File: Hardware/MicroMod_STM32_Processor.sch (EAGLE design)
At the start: 40 parts, among them J1 MICROMOD-2222, Q1 MOSFET_PCH-DMG2305UX-7, U1 STM32F405RGT6, U3 W25QXX128MBIT-6X5, Y1 12MHz, Y2 32.768kHz

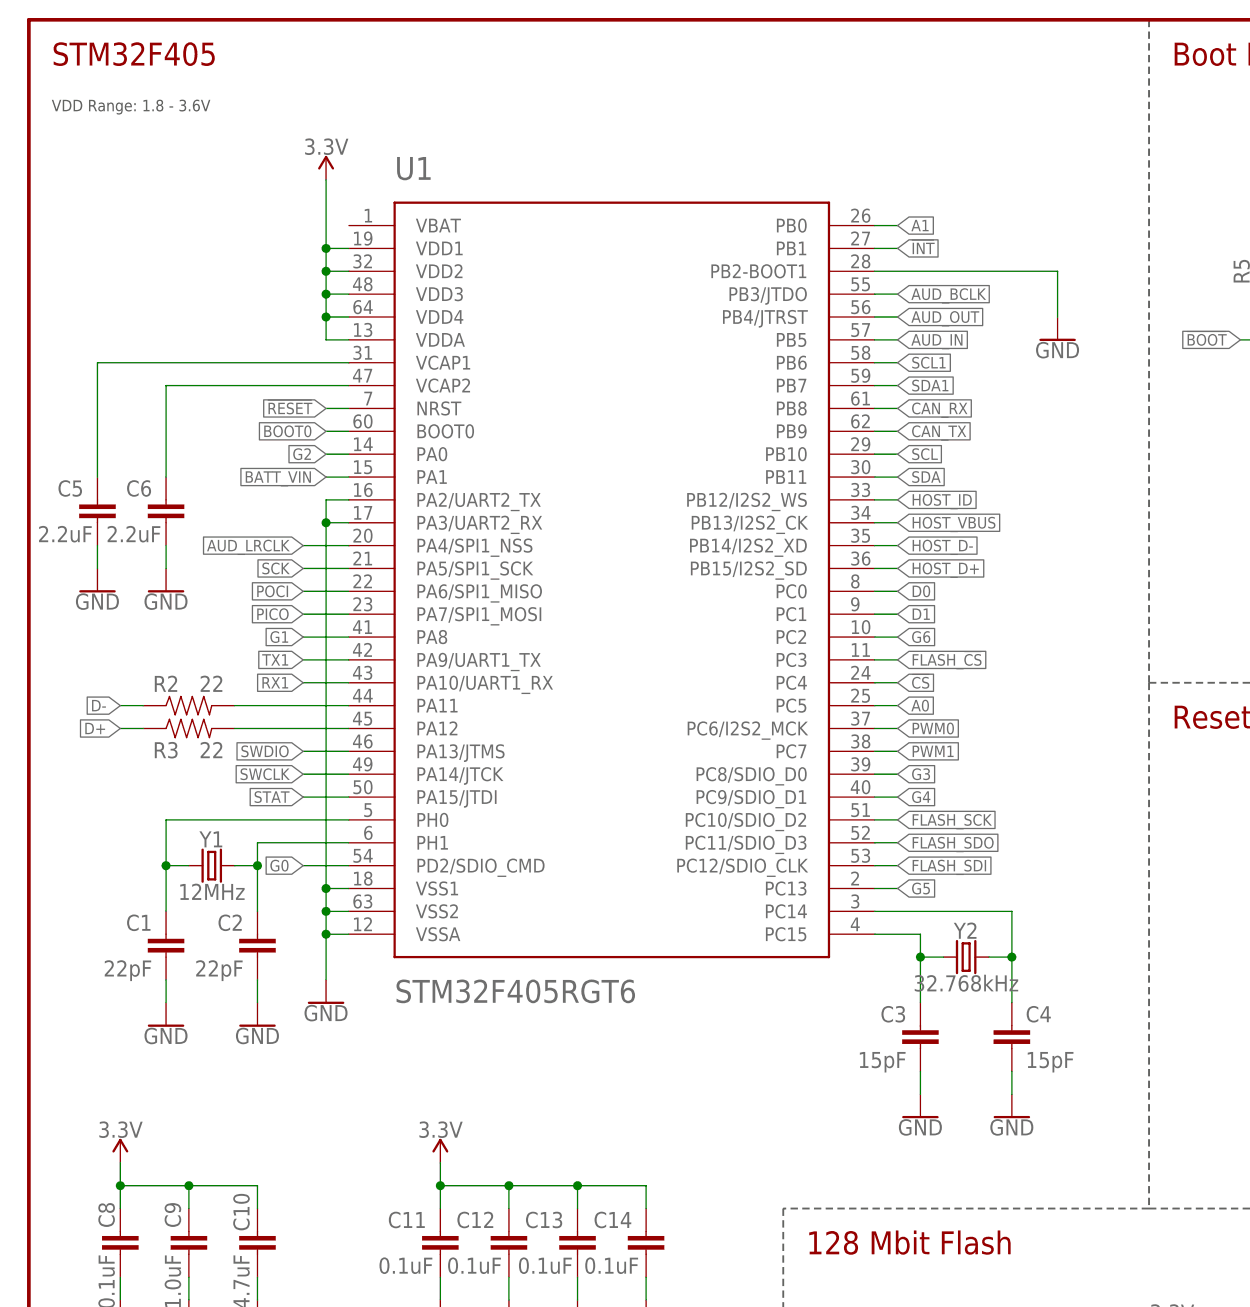
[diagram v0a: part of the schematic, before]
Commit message: Move some vias, replace STM32 with library part.
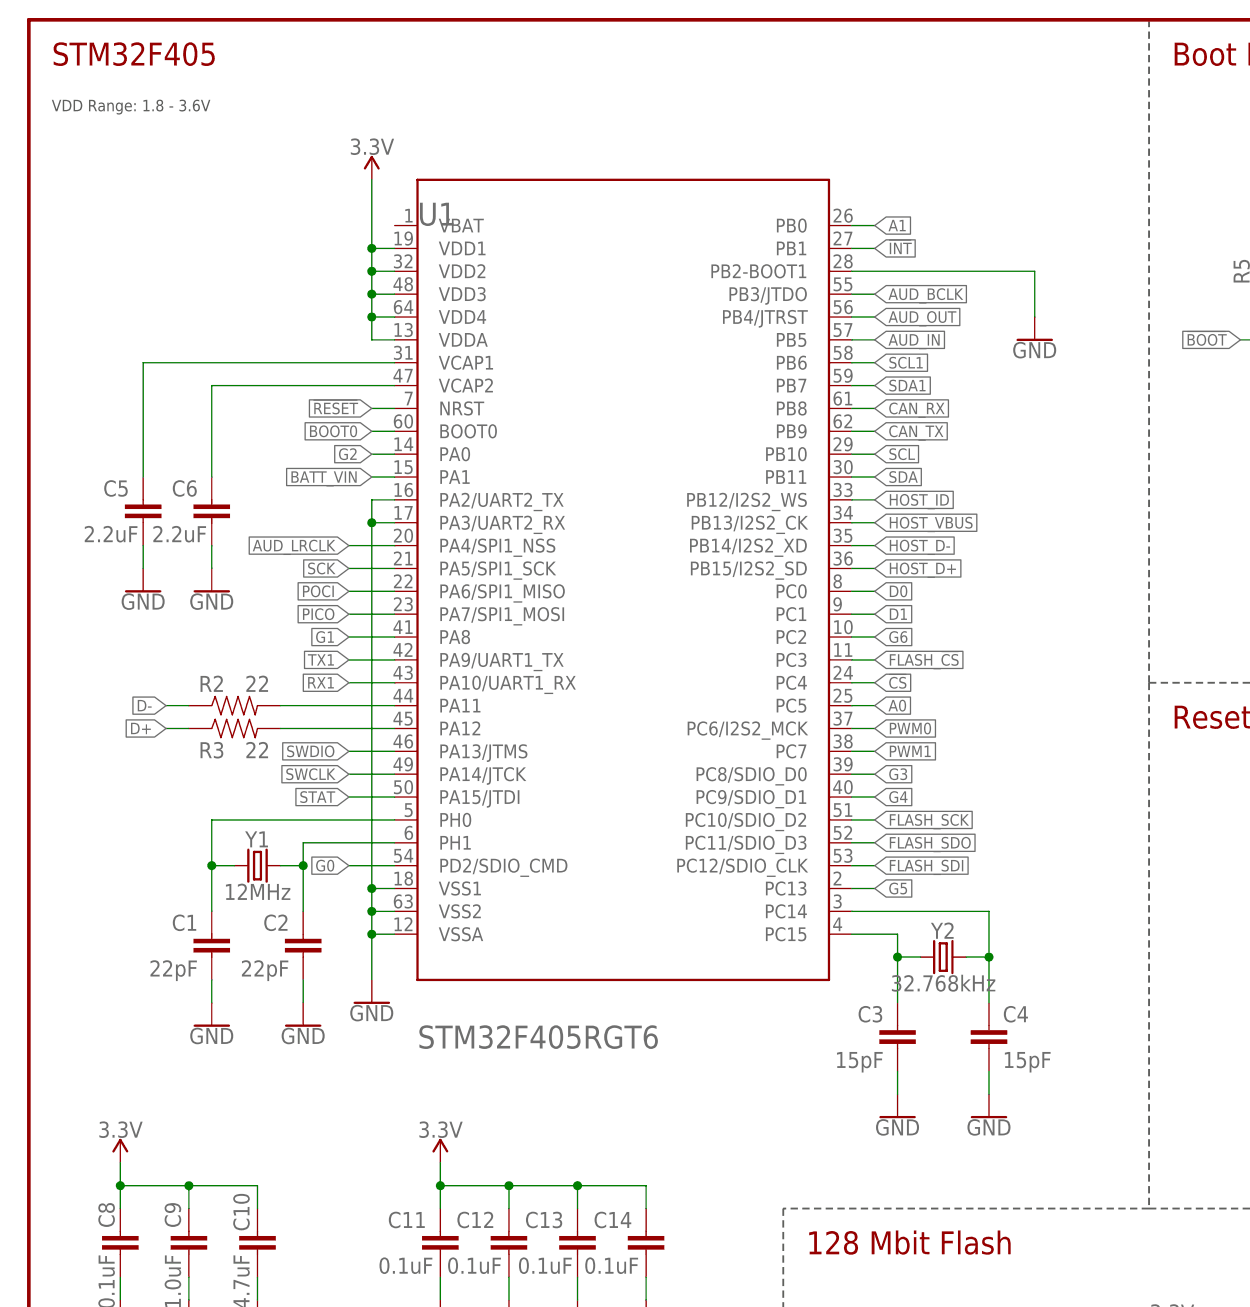
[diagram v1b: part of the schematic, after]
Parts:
- U1: device STM32_Temp:STM32F405RG -> SparkFun-IC-Microcontroller:STM32F405RG_LOGICAL
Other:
- moved on the sheet: C1, C2, C3, C4, C5, C6, R2, R3, U1, Y1, Y2

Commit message: Ready for v11 protos.
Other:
- note added: "v11"
- note removed: "v20"
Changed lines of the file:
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@@
 <text x="170.18" y="180.34" size="2.54" layer="94" font="vector" ratio="15">MicroMod Connector</text>
 <text x="2.54" y="180.34" size="2.54" layer="94" font="vector" ratio="15">STM32F405</text>
-<text x="238.76" y="7.62" size="2.54" layer="94" font="vector" ratio="15">v20</text>
+<text x="238.76" y="7.62" size="2.54" layer="94" font="vector" ratio="15">v11</text>
 <text x="168.148" y="11.684" size="2.54" layer="94" font="vector" ratio="7">Alex Wende</text>
 <wire x1="45.72" y1="27.94" x2="45.72" y2="0" width="0.2032" layer="97" style="shortdash"/>

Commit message: Update for v20 pushing to reds.
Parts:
- removed TP1, TP2, TP3, TP4: TEST-POINTTP_15TH_THRU, SparkFun-Connectors:TEST-POINTTP_15TH_THRU
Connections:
- net !RESET: no longer TP4.1
- net BOOT0: no longer TP3.1
- net RX1: no longer TP1.1
- net TX1: no longer TP2.1
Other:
- note added: "v20"
- note removed: "v11"
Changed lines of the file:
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@@
 <setting verticaltext="up"/>
 </settings>
-<grid distance="0.1" unitdist="inch" unit="inch" style="lines" multiple="1" display="yes" altdistance="0.01" altunitdist="inch" altunit="inch"/>
+<grid distance="0.1" unitdist="inch" unit="inch" style="lines" multiple="1" display="no" altdistance="0.01" altunitdist="inch" altunit="inch"/>
 <layers>
 <layer number="1" name="Top" color="4" fill="1" visible="no" active="no"/>
@@
 <part name="LOGO3" library="SparkFun-Aesthetics" deviceset="SFE_LOGO_NAME_FLAME" device=".1_INCH"/>
 <part name="GND8" library="SparkFun-PowerSymbols" deviceset="GND" device=""/>
-<part name="TP1" library="SparkFun-Connectors" deviceset="TEST-POINT" device="TP_15TH_THRU"/>
-<part name="TP2" library="SparkFun-Connectors" deviceset="TEST-POINT" device="TP_15TH_THRU"/>
-<part name="TP3" library="SparkFun-Connectors" deviceset="TEST-POINT" device="TP_15TH_THRU"/>
-<part name="TP4" library="SparkFun-Connectors" deviceset="TEST-POINT" device="TP_15TH_THRU"/>
 </parts>
 <sheets>
@@
 <text x="170.18" y="180.34" size="2.54" layer="94" font="vector" ratio="15">MicroMod Connector</text>
 <text x="2.54" y="180.34" size="2.54" layer="94" font="vector" ratio="15">STM32F405</text>
-<text x="238.76" y="7.62" size="2.54" layer="94" font="vector" ratio="15">v11</text>
+<text x="238.76" y="7.62" size="2.54" layer="94" font="vector" ratio="15">v20</text>
 <text x="168.148" y="11.684" size="2.54" layer="94" font="vector" ratio="7">Alex Wende</text>
 <wire x1="45.72" y1="27.94" x2="45.72" y2="0" width="0.2032" layer="97" style="shortdash"/>
@@
 <attribute name="VALUE" x="111.76" y="149.606" size="1.778" layer="96" font="vector" align="top-center"/>
 </instance>
-<instance part="TP1" gate="G$1" x="53.34" y="12.7" smashed="yes" rot="R90">
-<attribute name="NAME" x="50.8" y="17.78" size="1.778" layer="95" font="vector"/>
-<attribute name="VALUE" x="55.88" y="10.16" size="1.778" layer="96" font="vector" rot="R90" display="off"/>
-</instance>
-<instance part="TP2" gate="G$1" x="60.96" y="12.7" smashed="yes" rot="R90">
-<attribute name="NAME" x="58.42" y="17.78" size="1.778" layer="95" font="vector"/>
-<attribute name="VALUE" x="63.5" y="10.16" size="1.778" layer="96" font="vector" rot="R90" display="off"/>
-</instance>
-<instance part="TP3" gate="G$1" x="68.58" y="12.7" smashed="yes" rot="R90">
-<attribute name="NAME" x="66.04" y="17.78" size="1.778" layer="95" font="vector"/>
-<attribute name="VALUE" x="71.12" y="10.16" size="1.778" layer="96" font="vector" rot="R90" display="off"/>
-</instance>
-<instance part="TP4" gate="G$1" x="76.2" y="12.7" smashed="yes" rot="R90">
-<attribute name="NAME" x="73.66" y="17.78" size="1.778" layer="95" font="vector"/>
-<attribute name="VALUE" x="78.74" y="10.16" size="1.778" layer="96" font="vector" rot="R90" display="off"/>
-</instance>
 </instances>
 <busses>
@@
 <label x="147.32" y="81.28" size="1.27" layer="95" font="vector" xref="yes"/>
 </segment>
-<segment>
-<wire x1="76.2" y1="12.7" x2="76.2" y2="10.16" width="0.1524" layer="91"/>
-<label x="76.2" y="10.16" size="1.27" layer="95" font="vector" rot="R270" xref="yes"/>
-<pinref part="TP4" gate="G$1" pin="1"/>
-</segment>
 </net>
 <net name="BOOT0" class="0">
@@
 <label x="149.86" y="139.7" size="1.27" layer="95" font="vector" xref="yes"/>
 </segment>
-<segment>
-<wire x1="68.58" y1="12.7" x2="68.58" y2="10.16" width="0.1524" layer="91"/>
-<label x="68.58" y="10.16" size="1.27" layer="95" font="vector" rot="R270" xref="yes"/>
-<pinref part="TP3" gate="G$1" pin="1"/>
-</segment>
 </net>
 <net name="N$45" class="0">
@@
 <pinref part="U1" gate="G$1" pin="PA9/UART1_TX"/>
 </segment>
-<segment>
-<wire x1="60.96" y1="12.7" x2="60.96" y2="10.16" width="0.1524" layer="91"/>
-<label x="60.96" y="10.16" size="1.27" layer="95" font="vector" rot="R270" xref="yes"/>
-<pinref part="TP2" gate="G$1" pin="1"/>
-</segment>
 </net>
 <net name="RX1" class="0">
@@
 <pinref part="U1" gate="G$1" pin="PA10/UART1_RX"/>
 </segment>
-<segment>
-<wire x1="53.34" y1="12.7" x2="53.34" y2="10.16" width="0.1524" layer="91"/>
-<label x="53.34" y="10.16" size="1.27" layer="95" font="vector" rot="R270" xref="yes"/>
-<pinref part="TP1" gate="G$1" pin="1"/>
-</segment>
-</net>
+</net>

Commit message: Updated from current libraries. Removed R4.
Reset PUR unneeded per STM32 App Note AN4488.
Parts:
- Q1: value MOSFET_PCH-DMG2305UX-7 -> 20V/4.2A/52mΩ/1.4W
- R2, R3: value 22 -> 22Ω
- R4: value 5.1k -> DNP; device SparkFun-Resistors:5.1KOHM-0402T-1/16W-1% -> SparkFun-Resistors:DNP-0402T_NO_CREAM
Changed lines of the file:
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@@
 <part name="R12" library="SparkFun-Resistors" deviceset="1KOHM" device="-0402T-1/16W-1%" value="1k"/>
 <part name="GND35" library="SparkFun-PowerSymbols" deviceset="GND" device=""/>
-<part name="R2" library="SparkFun-Resistors" deviceset="22OHM" device="-0402T-1/16W-1%" value="22"/>
-<part name="R3" library="SparkFun-Resistors" deviceset="22OHM" device="-0402T-1/16W-1%" value="22"/>
-<part name="R4" library="SparkFun-Resistors" deviceset="5.1KOHM" device="-0402T-1/16W-1%" value="5.1k"/>
+<part name="R2" library="SparkFun-Resistors" deviceset="22OHM" device="-0402T-1/16W-1%" value="22Ω"/>
+<part name="R3" library="SparkFun-Resistors" deviceset="22OHM" device="-0402T-1/16W-1%" value="22Ω"/>
+<part name="R4" library="SparkFun-Resistors" deviceset="DNP" device="-0402T_NO_CREAM" value="DNP"/>
 <part name="C15" library="SparkFun-Capacitors" deviceset="0.1UF" device="-0402T-10V-10%-X7R" value="0.1uF"/>
 <part name="SUPPLY5" library="SparkFun-PowerSymbols" deviceset="3.3V" device=""/>
 <part name="GND16" library="SparkFun-PowerSymbols" deviceset="GND" device=""/>
 <part name="R5" library="SparkFun-Resistors" deviceset="100KOHM" device="-0402T-1/16W-1%" value="100k"/>
-<part name="Q1" library="SparkFun-DiscreteSemi" deviceset="MOSFET_PCH" device="-DMG2305UX-7" value=""/>
+<part name="Q1" library="SparkFun-DiscreteSemi" deviceset="MOSFET_PCH" device="-DMG2305UX-7" value="20V/4.2A/52mΩ/1.4W"/>
 <part name="SUPPLY6" library="SparkFun-PowerSymbols" deviceset="3.3V" device=""/>
 <part name="FD1" library="SparkFun-Aesthetics" deviceset="FIDUCIAL" device="UFIDUCIAL"/>
@@
 <attribute name="VALUE" x="25.4" y="105.156" size="1.778" layer="96" font="vector" align="top-center"/>
 </instance>
-<instance part="R4" gate="R1" x="144.78" y="88.9" smashed="yes" rot="R90">
+<instance part="R4" gate="G$1" x="144.78" y="88.9" smashed="yes" rot="R90">
 <attribute name="NAME" x="143.256" y="88.9" size="1.778" layer="95" font="vector" rot="R90" align="bottom-center"/>
 <attribute name="VALUE" x="146.304" y="88.9" size="1.778" layer="96" font="vector" rot="R90" align="top-center"/>
@@
 <segment>
 <pinref part="C15" gate="G$1" pin="1"/>
-<pinref part="R4" gate="R1" pin="1"/>
+<pinref part="R4" gate="G$1" pin="1"/>
 <wire x1="144.78" y1="78.74" x2="144.78" y2="81.28" width="0.1524" layer="91"/>
 <wire x1="144.78" y1="81.28" x2="144.78" y2="83.82" width="0.1524" layer="91"/>
@@
 </segment>
 <segment>
-<pinref part="R4" gate="R1" pin="2"/>
+<pinref part="R4" gate="G$1" pin="2"/>
 <wire x1="144.78" y1="93.98" x2="144.78" y2="96.52" width="0.1524" layer="91"/>
 <pinref part="SUPPLY5" gate="G$1" pin="3.3V"/>
@@
 which will not be processed correctly with this version.
 </note>
+<note version="8.3" severity="warning">
+Since Version 8.3, EAGLE supports URNs for individual library
+assets (packages, symbols, and devices). The URNs of those assets
+will not be understood (or retained) with this version.
+</note>
 </compatibility>

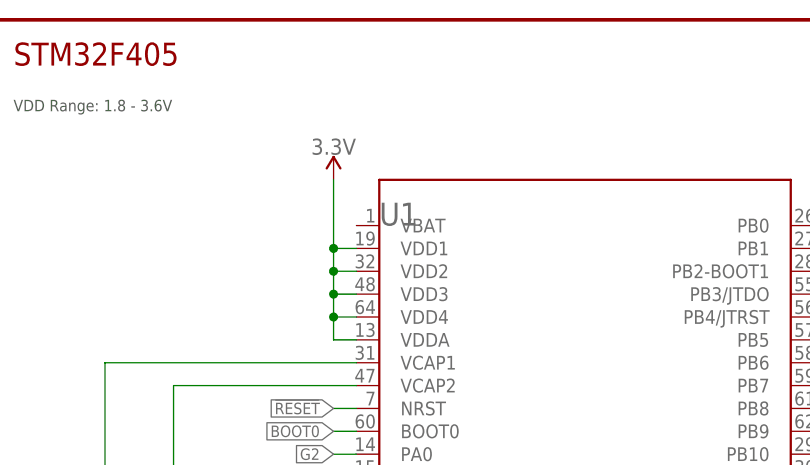
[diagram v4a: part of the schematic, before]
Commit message: Centered title, re-enabled layers.
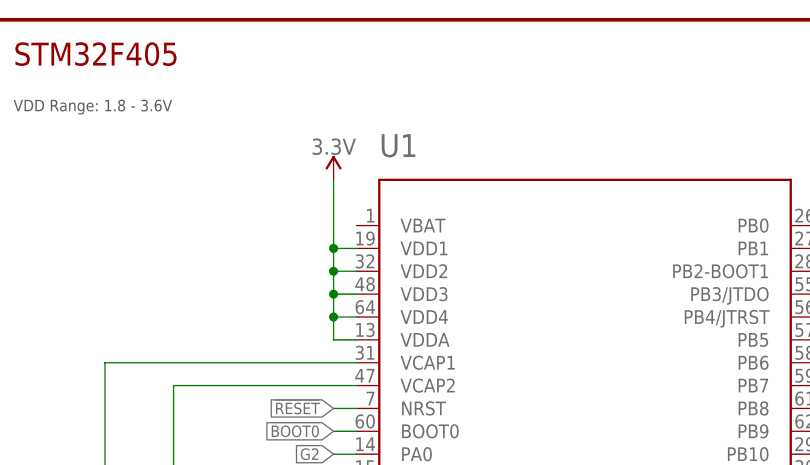
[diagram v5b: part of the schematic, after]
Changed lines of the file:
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@@
 </instance>
 <instance part="U1" gate="G$1" x="66.04" y="121.92" smashed="yes">
-<attribute name="NAME" x="43.18" y="162.56" size="2.54" layer="95" font="vector"/>
+<attribute name="NAME" x="43.18" y="170.18" size="2.54" layer="95" font="vector"/>
 <attribute name="VALUE" x="43.18" y="71.12" size="2.54" layer="96" font="vector"/>
 </instance>
